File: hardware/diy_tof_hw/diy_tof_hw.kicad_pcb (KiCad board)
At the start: 4 copper layers, 90 x 100 mm, 76 parts, among them IC1 TDC7200PWR, IC2 TDC7200PWR, IC21 74LVC1G08QW5-7, IC22 LMG1025QDEETQ1, J1 Conn_01x02_Pin, J2 Conn_01x03_Pin, J3 Conn_01x02_Pin, SW1 SW_Nidec_CAS-120A1, SW2 SW_Nidec_CAS-120A1, U1 NUCLEO-F042K6, U2 OPA858xDSG, U3 TLV3501AIDBV, X1 SG-5032CAN

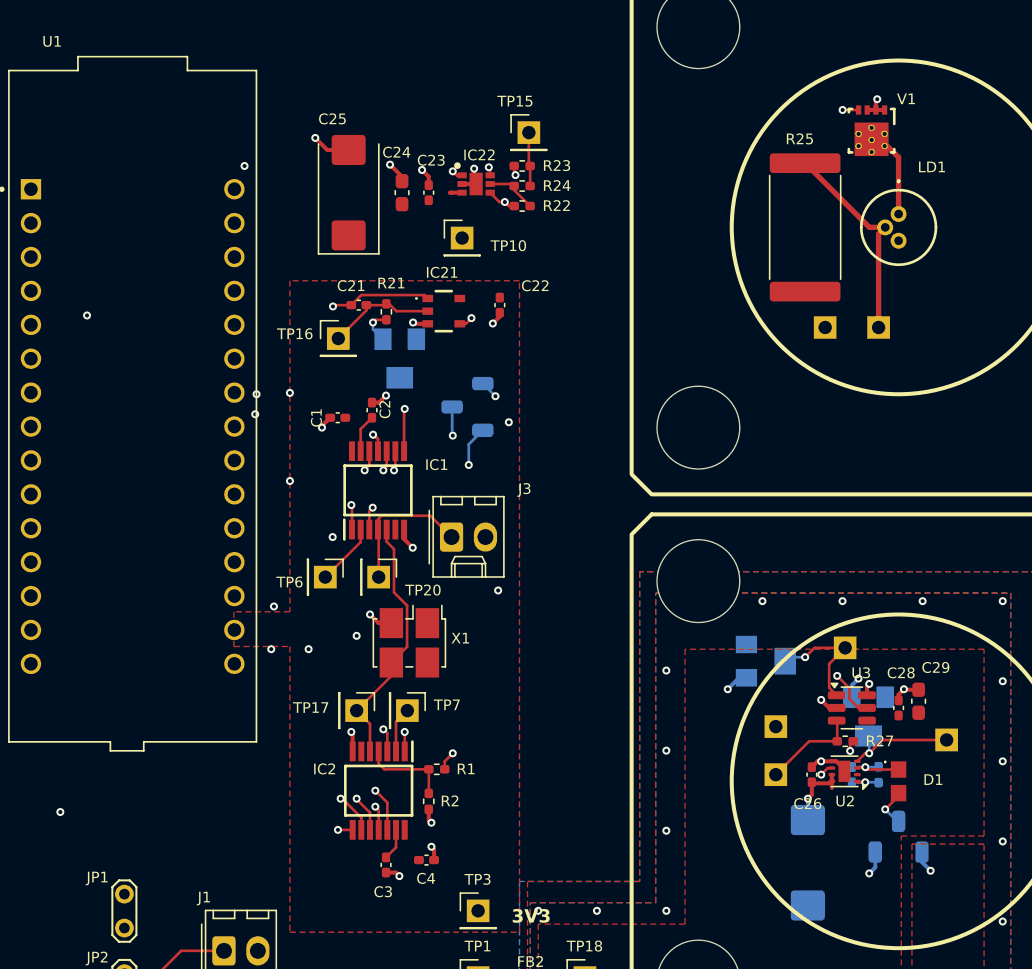
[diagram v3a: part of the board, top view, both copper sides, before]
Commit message: [hardware] changed footprint of R25 to 0603, updated some ICs footprint models in order to comply with e.g. via hole size constraints
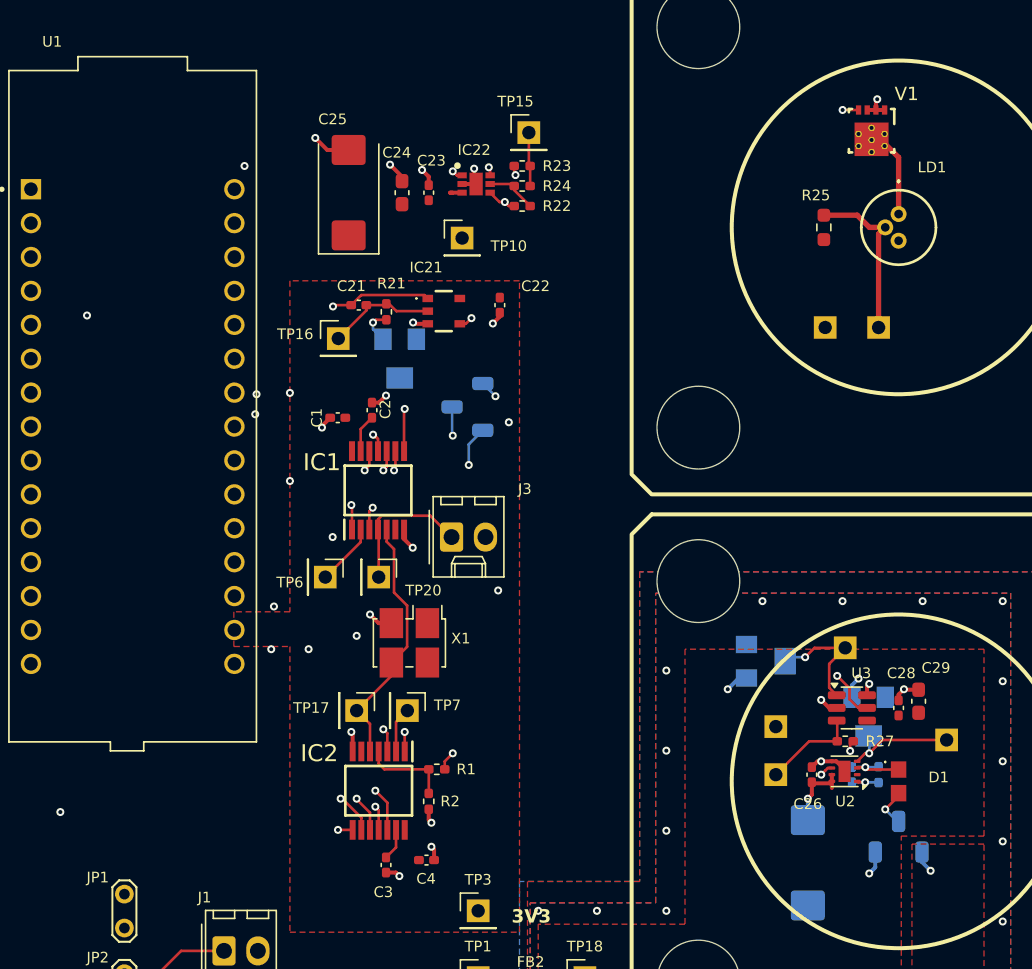
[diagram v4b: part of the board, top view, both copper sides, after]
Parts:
- R25: value XXX -> 75; footprint Resistor_SMD:R_4020_10251Metric -> Resistor_SMD:R_0603_1608Metric_Pad0.98x0.95mm_HandSolder
- moved R25 1.40 mm to (109.4, 58.8)
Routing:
- net Net-(TP9-Pin_1): track 15.7 -> 12.7 mm
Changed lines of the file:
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@@
 		)
 		(property "Value" "100n"
-			(at 0 1.16 360)
+			(at 0 1.16 0)
 			(layer "F.Fab")
 			(effects
@@
 		)
 		(fp_text user "${REFERENCE}"
-			(at 0 0 360)
+			(at 0 0 0)
 			(layer "F.Fab")
 			(effects
@@
 		(tags "CONN DEV")
 		(property "Reference" "JP1"
-			(at -1.25 2 360)
+			(at -1.25 2 0)
 			(unlocked yes)
 			(layer "F.SilkS")
@@
 		)
 	)
-	(footprint "Resistor_SMD:R_4020_10251Metric"
+	(footprint "Resistor_SMD:R_0603_1608Metric_Pad0.98x0.95mm_HandSolder"
 		(layer "F.Cu")
-		(at 108 58.8 90)
-		(descr "Resistor SMD 4020 (10251 Metric), square (rectangular) end terminal, IPC_7351 nominal, (Body size source: http://datasheet.octopart.com/HVC0603T5004FET-Ohmite-datasheet-26699797.pdf), generated with kicad-footprint-generator")
-		(tags "resistor")
+		(at 109.4 58.8 90)
+		(descr "Resistor SMD 0603 (1608 Metric), square (rectangular) end terminal, IPC_7351 nominal with elongated pad for handsoldering. (Body size source: IPC-SM-782 page 72, https://www.pcb-3d.com/wordpress/wp-content/uploads/ipc-sm-782a_amendment_1_and_2.pdf), generated with kicad-footprint-generator")
+		(tags "resistor handsolder")
 		(property "Reference" "R25"
-			(at 6.6 -0.4 0)
-			(unlocked yes)
+			(at 2.4 -0.6 180)
 			(layer "F.SilkS")
 			(effects
@@
 			)
 		)
-		(property "Value" "XXX"
-			(at 0 3.6 90)
+		(property "Value" "75"
+			(at 0 1.43 90)
 			(layer "F.Fab")
 			(effects
@@
 			)
 		)
-		(property "Footprint" "Resistor_SMD:R_4020_10251Metric"
+		(property "Footprint" "Resistor_SMD:R_0603_1608Metric_Pad0.98x0.95mm_HandSolder"
 			(at 0 0 90)
 			(unlocked yes)
@@
 		(attr smd)
 		(fp_line
-			(start -3.886252 -2.66)
-			(end 3.886252 -2.66)
+			(start -0.254724 -0.5225)
+			(end 0.254724 -0.5225)
 			(stroke
 				(width 0.12)
@@
 		)
 		(fp_line
-			(start -3.886252 2.66)
-			(end 3.886252 2.66)
+			(start -0.254724 0.5225)
+			(end 0.254724 0.5225)
 			(stroke
 				(width 0.12)
@@
 		)
 		(fp_line
-			(start 5.8 -2.9)
-			(end 5.8 2.9)
+			(start 1.65 -0.73)
+			(end 1.65 0.73)
 			(stroke
 				(width 0.05)
@@
 		)
 		(fp_line
-			(start -5.8 -2.9)
-			(end 5.8 -2.9)
+			(start -1.65 -0.73)
+			(end 1.65 -0.73)
 			(stroke
 				(width 0.05)
@@
 		)
 		(fp_line
-			(start 5.8 2.9)
-			(end -5.8 2.9)
+			(start 1.65 0.73)
+			(end -1.65 0.73)
 			(stroke
 				(width 0.05)
@@
 		)
 		(fp_line
-			(start -5.8 2.9)
-			(end -5.8 -2.9)
+			(start -1.65 0.73)
+			(end -1.65 -0.73)
 			(stroke
 				(width 0.05)
@@
 		)
 		(fp_line
-			(start 5.1 -2.55)
-			(end 5.1 2.55)
+			(start 0.8 -0.4125)
+			(end 0.8 0.4125)
 			(stroke
 				(width 0.1)
@@
 		)
 		(fp_line
-			(start -5.1 -2.55)
-			(end 5.1 -2.55)
+			(start -0.8 -0.4125)
+			(end 0.8 -0.4125)
 			(stroke
 				(width 0.1)
@@
 		)
 		(fp_line
-			(start 5.1 2.55)
-			(end -5.1 2.55)
+			(start 0.8 0.4125)
+			(end -0.8 0.4125)
 			(stroke
 				(width 0.1)
@@
 		)
 		(fp_line
-			(start -5.1 2.55)
-			(end -5.1 -2.55)
+			(start -0.8 0.4125)
+			(end -0.8 -0.4125)
 			(stroke
 				(width 0.1)
@@
 			(effects
 				(font
-					(size 1 1)
-					(thickness 0.15)
+					(size 0.4 0.4)
+					(thickness 0.06)
 				)
 			)
 		)
 		(pad "1" smd roundrect
-			(at -4.8125 0 90)
-			(size 1.475 5.3)
+			(at -0.9125 0 90)
+			(size 0.975 0.95)
 			(layers "F.Cu" "F.Paste" "F.Mask")
-			(roundrect_rratio 0.169492)
+			(roundrect_rratio 0.25)
 			(net 25 "5V")
 			(pintype "passive")
 		)
 		(pad "2" smd roundrect
-			(at 4.8125 0 90)
-			(size 1.475 5.3)
+			(at 0.9125 0 90)
+			(size 0.975 0.95)
 			(layers "F.Cu" "F.Paste" "F.Mask")
-			(roundrect_rratio 0.169492)
+			(roundrect_rratio 0.25)
 			(net 57 "Net-(TP9-Pin_1)")
 			(pintype "passive")
 		)
-		(model "${KICAD8_3DMODEL_DIR}/Resistor_SMD.3dshapes/R_4020_10251Metric.wrl"
+		(model "${KICAD8_3DMODEL_DIR}/Resistor_SMD.3dshapes/R_0603_1608Metric.wrl"
 			(offset
 				(xyz 0 0 0)
@@
 		(tags "resistor handsolder")
 		(property "Reference" "R1"
-			(at -2.1975 0 360)
+			(at -2.1975 0 0)
 			(unlocked yes)
 			(layer "F.SilkS")
@@
 		)
 		(property "Value" "20k"
-			(at 0 1.17 360)
+			(at 0 1.17 0)
 			(layer "F.Fab")
 			(effects
@@
 		)
 		(fp_text user "${REFERENCE}"
-			(at 0 0 360)
+			(at 0 0 0)
 			(layer "F.Fab")
 			(effects
@@
 		)
 		(fp_text user "${REFERENCE}"
-			(at 0 0 360)
+			(at 0 0 0)
 			(layer "F.Fab")
 			(effects
@@
 		)
 		(fp_text user "${REFERENCE}"
-			(at 0 0 360)
+			(at 0 0 0)
 			(layer "F.Fab")
 			(effects
@@
 		(tags "Integrated Circuit")
 		(property "Reference" "IC22"
-			(at 0.25 -2.15 0)
-			(unlocked yes)
+			(at -0.15 -2.55 0)
 			(layer "F.SilkS")
 			(effects
@@
 		(tags "SMD SMT crystal oscillator hand-soldering")
 		(property "Reference" "X1"
-			(at -3.85 0.325 360)
+			(at -3.85 0.325 0)
 			(unlocked yes)
 			(layer "F.SilkS")
@@
 		)
 		(property "Value" "SG-5032CAN"
-			(at 0 3.6 360)
+			(at 0 3.6 0)
 			(layer "F.Fab")
 			(effects
@@
 		)
 		(fp_text user "${REFERENCE}"
-			(at 0 0 360)
+			(at 0 0 0)
 			(layer "F.Fab")
 			(effects
@@
 		(tags "Integrated Circuit")
 		(property "Reference" "IC21"
-			(at 2.875 -0.125 0)
+			(at 3.275 -1.325 0)
 			(unlocked yes)
 			(layer "F.SilkS")
@@
 				(font
 					(size 0.8 0.8)
-					(thickness 0.254)
+					(thickness 0.2)
 				)
 			)
@@
 		(tags "Integrated Circuit")
 		(property "Reference" "IC2"
-			(at -1.6 4.05 0)
-			(unlocked yes)
+			(at -2.8 4.45 0)
 			(layer "F.SilkS")
 			(effects
 				(font
-					(size 0.8 0.8)
+					(size 1.27 1.27)
 					(thickness 0.254)
 				)
@@
 		)
 		(fp_text user "${REFERENCE}"
-			(at 0 0 360)
+			(at 0 0 0)
 			(layer "F.Fab")
 			(effects
@@
 		)
 		(fp_text user "${REFERENCE}"
-			(at 0 0 360)
+			(at 0 0 0)
 			(layer "F.Fab")
 			(effects
@@
 		(tags "Photodiode")
 		(property "Reference" "D1"
-			(at 2.6 -0.1 0)
-			(unlocked yes)
+			(at 3 -0.3 0)
 			(layer "F.SilkS")
 			(effects
@@
 		)
 		(property "Value" "Conn_01x02_Pin"
-			(at 1.27 4.08 360)
+			(at 1.27 4.08 0)
 			(layer "F.Fab")
 			(effects
@@
 		)
 		(fp_text user "${REFERENCE}"
-			(at 1.27 -2.22 360)
+			(at 1.27 -2.22 0)
 			(layer "F.Fab")
 			(effects
@@
 		)
 		(property "Value" "100n"
-			(at 0 1.16 360)
+			(at 0 1.16 0)
 			(layer "F.Fab")
 			(effects
@@
 		)
 		(fp_text user "${REFERENCE}"
-			(at 0 0 360)
+			(at 0 0 0)
 			(layer "F.Fab")
 			(effects
@@
 		(tags "Integrated Circuit")
 		(property "Reference" "IC1"
-			(at 1.9 4.4 0)
-			(unlocked yes)
+			(at 2.1 -4.2 180)
 			(layer "F.SilkS")
 			(effects
 				(font
-					(size 0.8 0.8)
+					(size 1.27 1.27)
 					(thickness 0.254)
 				)
@@
 		(tags "CSD17578Q3A ")
 		(property "Reference" "V1"
-			(at -2.354999 -2.625001 0)
+			(at -2.754999 -2.625001 0)
 			(unlocked yes)
 			(layer "F.SilkS")
 			(effects
 				(font
-					(size 0.8 0.8)
+					(size 1 1)
 					(thickness 0.15)
 				)
@@
 		)
 		(property "Footprint" "DNH0008A"
-			(at 0 0 90)
+			(at 0 0 -90)
 			(layer "F.Fab")
 			(hide yes)
@@
 		)
 		(property "Datasheet" "CSD17578Q3A"
-			(at 0 0 90)
+			(at 0 0 -90)
 			(layer "F.Fab")
 			(hide yes)
@@
 		)
 		(property "Description" ""
-			(at 0 0 90)
+			(at 0 0 -90)
 			(layer "F.Fab")
 			(hide yes)
@@
 		)
 		(fp_text user "Designator291"
-			(at -1.651 -3.0734 -90)
+			(at 0.08 2.61 -90)
 			(unlocked yes)
 			(layer "F.SilkS")
@@
 		)
 		(pad "9" thru_hole circle
-			(at 1.15 -0.974999)
+			(at 1.15 -0.974999 270)
 			(size 0.499999 0.499999)
 			(drill 0.3)
@@
 		(tags "Potentiometer vertical Bourns 3224W")
 		(property "Reference" "RV22"
-			(at -1.45 3.25 360)
+			(at -1.45 3.25 0)
 			(unlocked yes)
 			(layer "B.SilkS")
@@
 		)
 		(property "Value" "1k"
-			(at 0 -3.5 360)
+			(at 0 -3.5 0)
 			(layer "B.Fab")
 			(effects
@@
 		)
 		(fp_text user "${REFERENCE}"
-			(at 0.6 0 360)
+			(at 0.6 0 0)
 			(layer "B.Fab")
 			(effects
@@
 	)
 	(segment
-		(start 112.8125 58.8)
-		(end 114 58.8)
+		(start 109.4 57.8875)
+		(end 111.9 57.8875)
 		(width 0.4)
 		(layer "F.Cu")
@@
 	)
 	(segment
-		(start 113.5 59.3)
+		(start 112.8125 58.8)
 		(end 114 58.8)
 		(width 0.4)
@@
 	)
 	(segment
-		(start 108 53.9875)
+		(start 111.9 57.8875)
 		(end 112.8125 58.8)
 		(width 0.4)
 		(layer "F.Cu")
+		(net 57)
+	)
+	(segment
+		(start 113.5 59.3)
+		(end 114 58.8)
+		(width 0.4)
+		(layer "F.Cu")

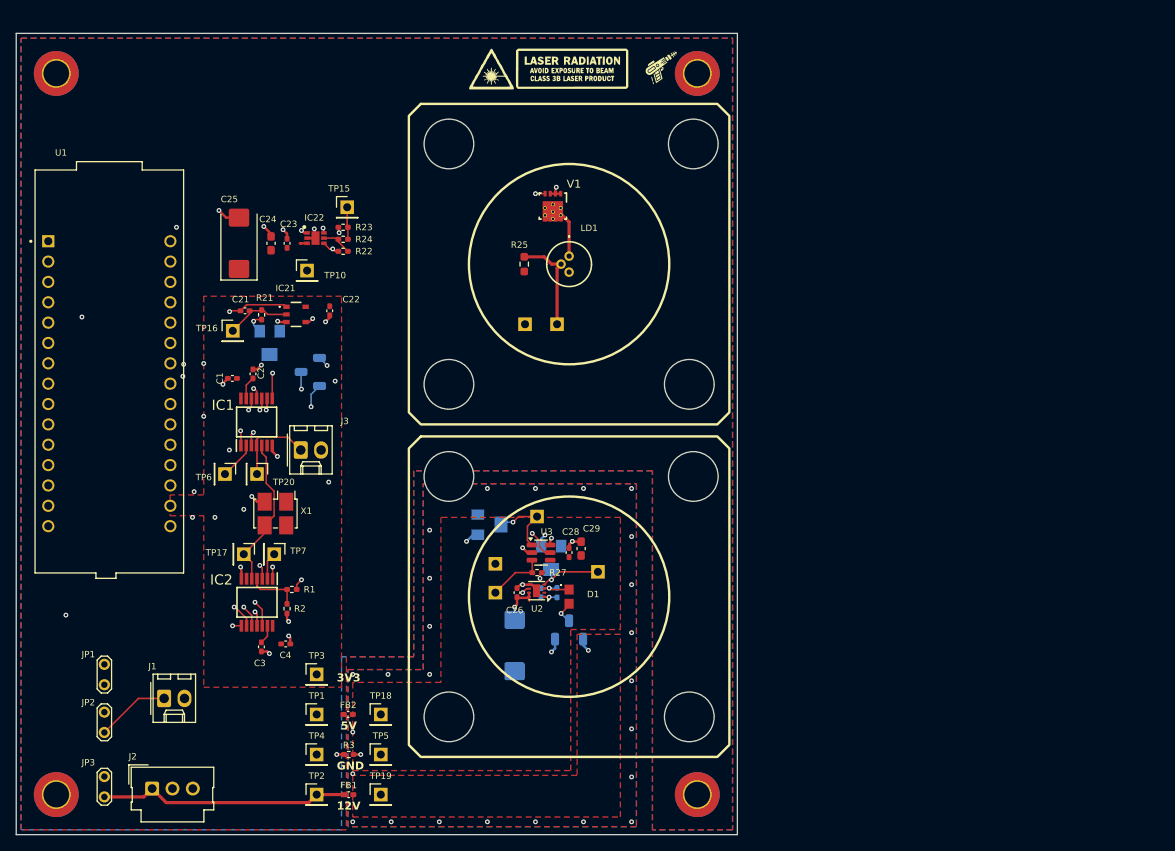
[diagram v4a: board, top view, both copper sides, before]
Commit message: [hardware] review findings  - moved powerplanes to layer In1  - added ground planes on all other layers  - rerouting of signals around the nucleo board, leaving enough space for ground fills
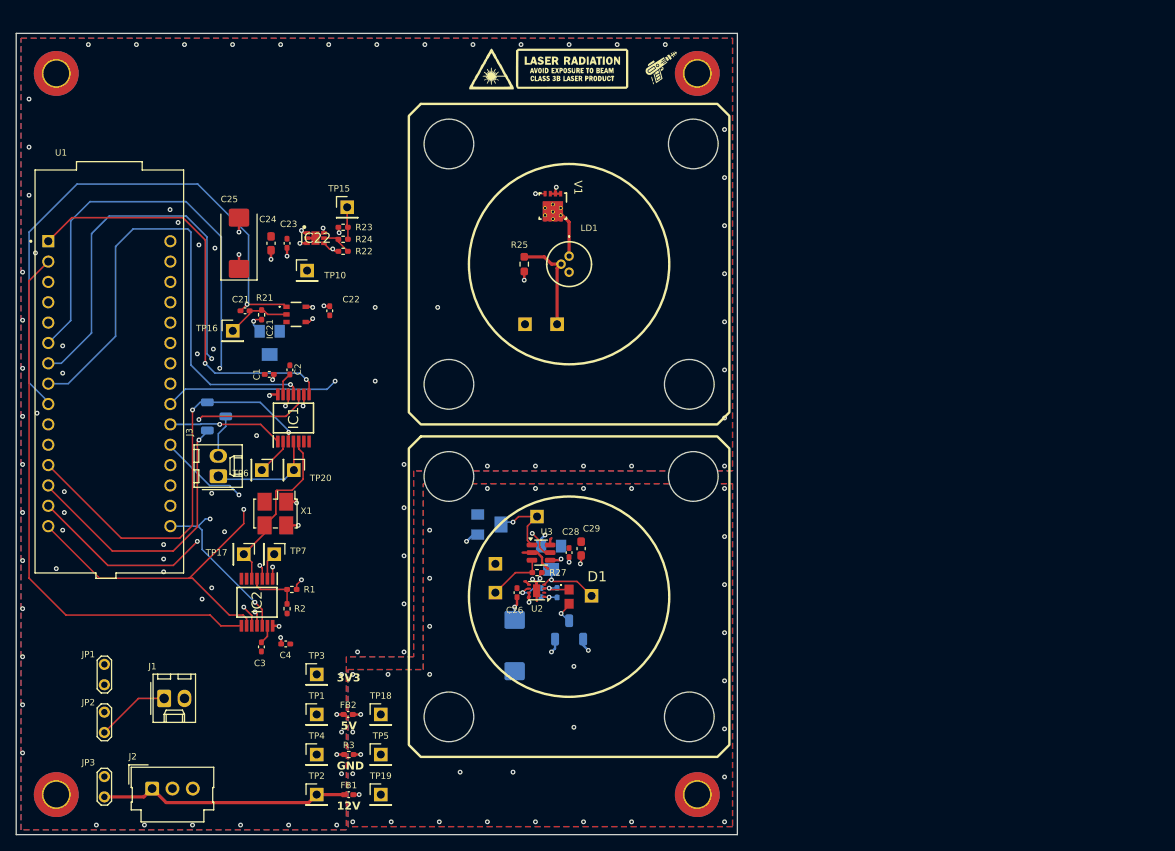
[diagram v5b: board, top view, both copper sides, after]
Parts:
- moved SW1 12.9 mm to (71.0, 77.8), turned to 0 degrees
- moved J3 10.8 mm to (71.2, 85.3), turned to 90 degrees
- moved C2 4.63 mm to (80.2, 72.0)
- moved TP20 4.63 mm to (80.7, 84.5)
- moved TP6 4.63 mm to (76.7, 84.5)
- moved C1 4.63 mm to (77.6, 72.6)
- moved IC1 4.63 mm to (80.6, 78.0)
- moved TP13 3.10 mm to (117.8, 100.2)
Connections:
- H4 pad 1: GND -> unconnected-(H4-Pad1)_2
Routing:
- net /Power_Nucleo_TDC/spi_cs_opt: track 56.3 -> 93.2 mm
- net /Power_Nucleo_TDC/spi_cs_ele: track 27.9 -> 64.1 mm
- net /Power_Nucleo_TDC/start_opt: track 52.3 -> 87.9 mm
- net /Optoelectronics/LD_pulse: track 38.9 -> 69.9 mm, vias 2 -> 1
- net GND: track 24.4 -> 7.25 mm, vias 16 -> 82
- net /Power_Nucleo_TDC/stop_ele: track 52.3 -> 35.8 mm, vias 2 -> 1
- net /Power_Nucleo_TDC/start_ele: track 40.6 -> 52.1 mm
- net /Power_Nucleo_TDC/spi_mosi: track 57.7 -> 66.3 mm, vias 4 -> 3
- net 3V3: track 0.00 -> 8.00 mm, vias 0 -> 8
- net 5V: track 1.10 -> 7.01 mm, vias 0 -> 6
- net /Power_Nucleo_TDC/int_ele: track 47.2 -> 52.8 mm, vias 3 -> 2
- net Net-(J3-Pin_2): track 10.8 -> 5.32 mm, vias 1 -> 0
- net /Power_Nucleo_TDC/spi_clk: track 38.7 -> 42.9 mm
- net /Power_Nucleo_TDC/TDC_ele_enable: track 11.0 -> 14.3 mm
- net 5V_LN: track 10.7 -> 13.8 mm, vias 4 -> 9
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- added copper zone on In1.Cu, net 12V_LN
- added copper zone on In1.Cu, net 3V3
- added copper zone on In1.Cu, net 5V
- added copper zone on In1.Cu, net 5V_LN
- added copper zone on F.Cu, net GND
- added copper zone on In2.Cu, net GND
- added copper zone on In2.Cu, net GNDA
- removed copper zone on F.Cu, net 12V_LN
- removed copper zone on F.Cu, net 3V3
- removed copper zone on F.Cu, net 5V
- removed copper zone on F.Cu, net 5V_LN

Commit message: [hardware] further review findings  - adjusted some more traces  - one via per power pad  - added caps for a pi filter (dnp)  - added pullups for the CS signals of both TDCs
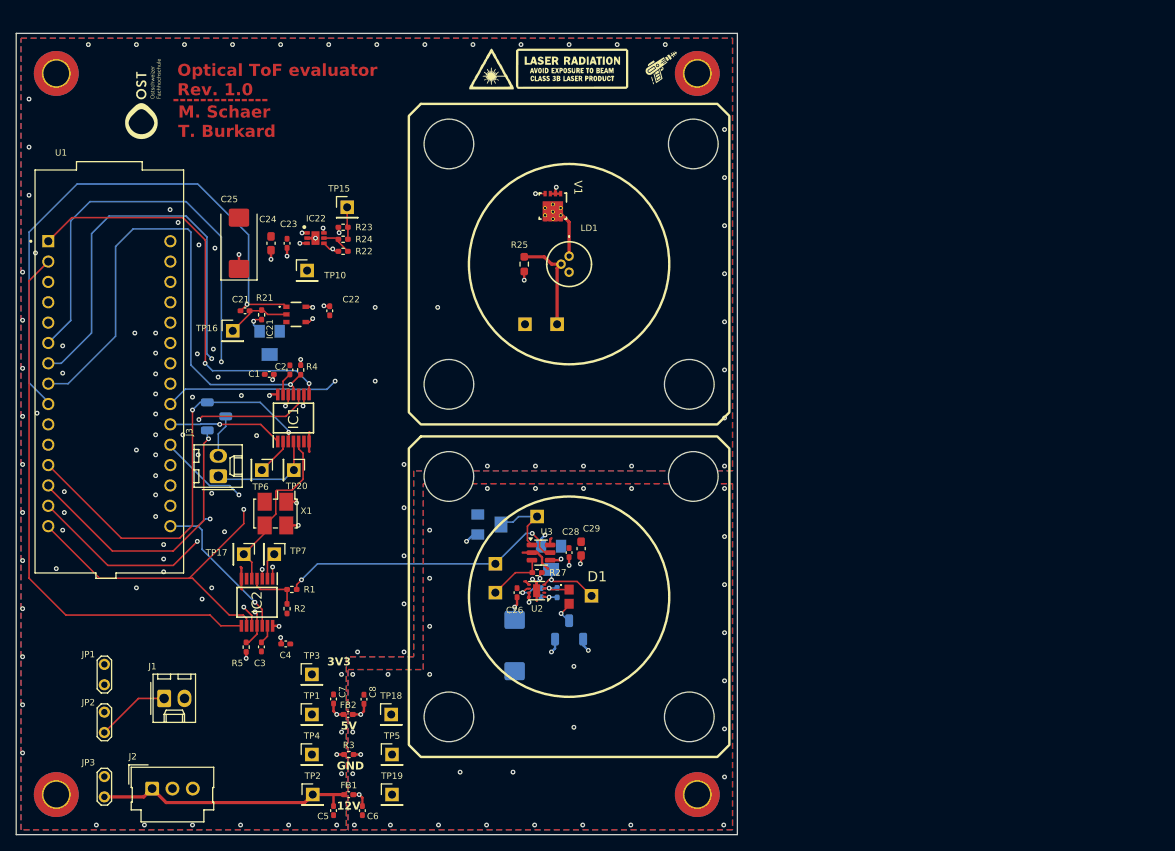
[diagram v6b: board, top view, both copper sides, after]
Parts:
- added C5: 1u, Capacitor_SMD:C_0402_1005Metric_Pad0.74x0.62mm_HandSolder, F.Cu at (85.6, 127.0)
- added C6: 1u, Capacitor_SMD:C_0402_1005Metric_Pad0.74x0.62mm_HandSolder, F.Cu at (89.2, 127.0)
- added C7: 1u, Capacitor_SMD:C_0402_1005Metric_Pad0.74x0.62mm_HandSolder, F.Cu at (85.6, 113.1)
- added C8: 1u, Capacitor_SMD:C_0402_1005Metric_Pad0.74x0.62mm_HandSolder, F.Cu at (89.4, 113.1)
- added G***: LOGO, LOGO, F.Cu at (61.8, 38.2)
- added R4: 20k, Resistor_SMD:R_0402_1005Metric_Pad0.72x0.64mm_HandSolder, F.Cu at (81.5, 72.0)
- added R5: 20k, Resistor_SMD:R_0402_1005Metric_Pad0.72x0.64mm_HandSolder, F.Cu at (74.7, 106.6)
- LD1: value ~ -> RLD65NZX1
- moved TP19 1.40 mm to (92.9, 125.0)
- moved TP5 1.40 mm to (92.9, 120.0)
- moved TP18 1.30 mm to (92.8, 115.0)
- moved TP1 0.60 mm to (82.9, 115.0)
- moved TP3 0.60 mm to (82.9, 110.0)
- moved TP4 0.60 mm to (82.9, 120.0)
- moved TP2 0.50 mm to (83.0, 125.0)
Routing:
- net GND: track 7.25 -> 10.8 mm, vias 82 -> 100
- net /Power_Nucleo_TDC/spi_cs_opt: track 93.2 -> 96.0 mm
- net 5V_LN: track 13.8 -> 15.7 mm
- net /Power_Nucleo_TDC/spi_cs_ele: track 64.1 -> 65.9 mm
- net 12V_LN: track 2.40 -> 4.00 mm
- net 5V: track 7.01 -> 8.54 mm
- net 3V3: track 8.00 -> 9.51 mm, vias 8 -> 10
- net 12V: track 31.5 -> 32.9 mm
- net /Power_Nucleo_TDC/12_nuc: track 71.2 -> 72.5 mm
- net Net-(IC21-Y): track 13.5 -> 12.9 mm
- net Net-(TP14-Pin_1): vias 1 -> 0
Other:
- board text added: "--------------"
- board text added: "M. Schaer T. Burkard"
- board text added: "Optical ToF evaluator Rev. 1.0"
